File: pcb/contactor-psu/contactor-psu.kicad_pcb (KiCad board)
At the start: 2 copper layers, 44.1 x 24 mm, 4 parts, among them J1 Conn_01x02_Socket

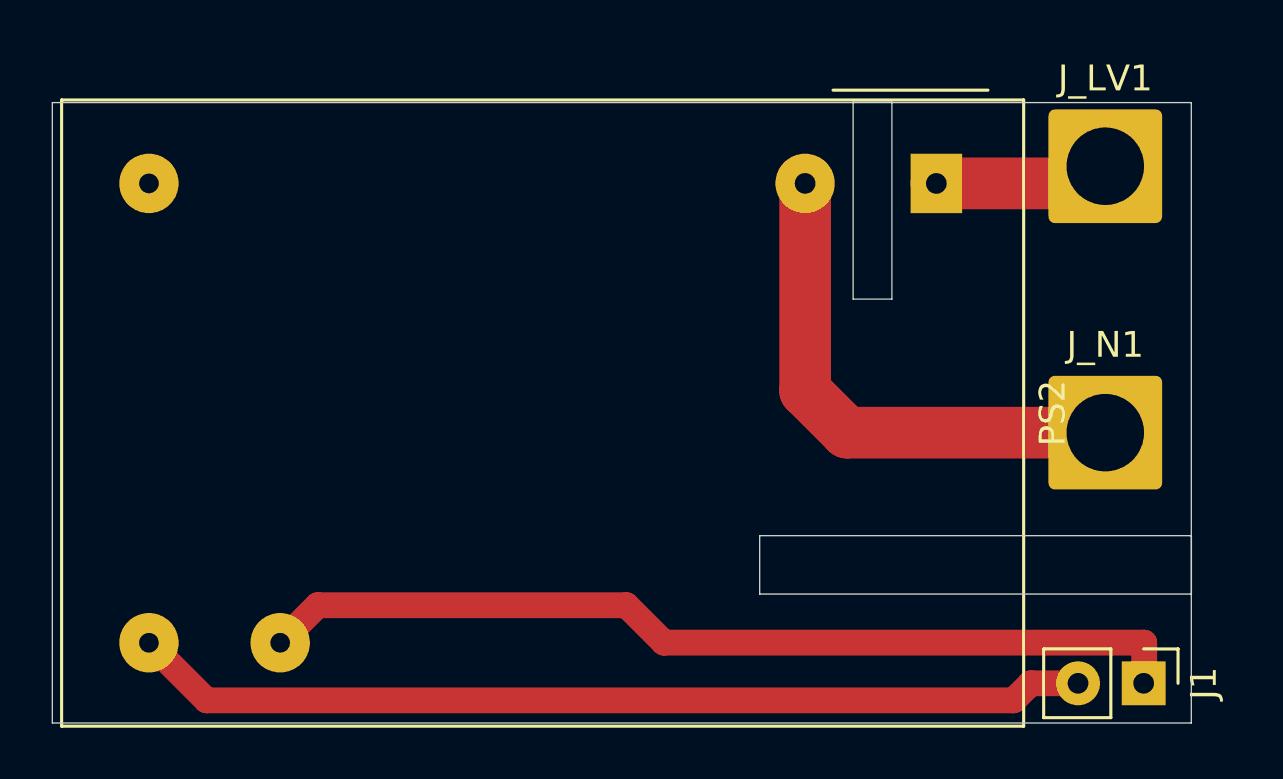
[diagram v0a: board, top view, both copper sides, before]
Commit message: Fixes to relief, JST connectors for SMT board
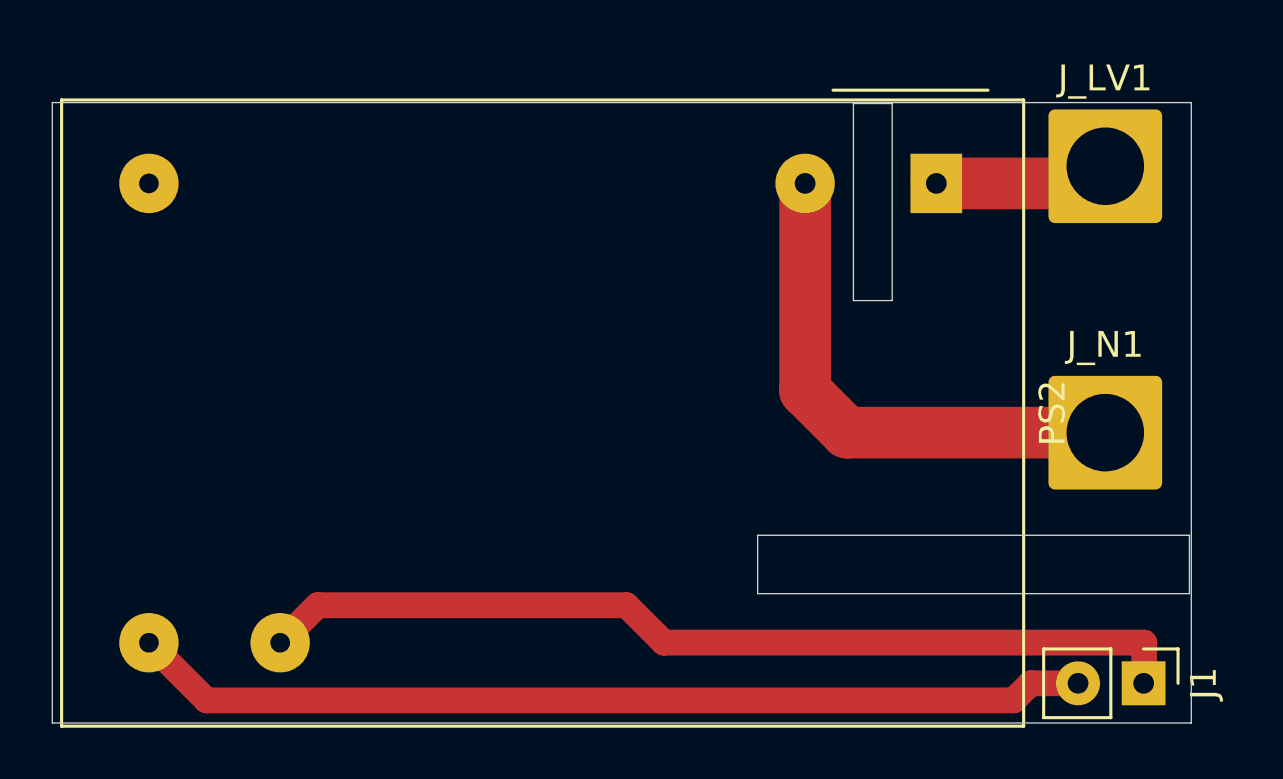
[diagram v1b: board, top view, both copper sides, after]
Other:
- outline, holes or cut-outs redrawn
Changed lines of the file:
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@@
 			(size 4.4 4.4)
 			(drill 3)
-			(layers "*.Cu" "*.Mask")
+			(layers "*.Cu" "*.Mask" "In1.Cu" "In2.Cu" "In3.Cu" "In4.Cu" "In5.Cu" "In6.Cu"
+				"In7.Cu" "In8.Cu" "In9.Cu" "In10.Cu" "In11.Cu" "In12.Cu" "In13.Cu" "In14.Cu"
+				"In15.Cu" "In16.Cu" "In17.Cu" "In18.Cu" "In19.Cu" "In20.Cu" "In21.Cu"
+				"In22.Cu" "In23.Cu" "In24.Cu" "In25.Cu" "In26.Cu" "In27.Cu" "In28.Cu"
+				"In29.Cu" "In30.Cu"
+			)
 			(remove_unused_layers no)
 			(roundrect_rratio 0.056818)
@@
 			(size 2.3 2)
 			(drill 0.8)
-			(layers "*.Cu" "*.Mask")
+			(layers "*.Cu" "*.Mask" "In1.Cu" "In2.Cu" "In3.Cu" "In4.Cu" "In5.Cu" "In6.Cu"
+				"In7.Cu" "In8.Cu" "In9.Cu" "In10.Cu" "In11.Cu" "In12.Cu" "In13.Cu" "In14.Cu"
+				"In15.Cu" "In16.Cu" "In17.Cu" "In18.Cu" "In19.Cu" "In20.Cu" "In21.Cu"
+				"In22.Cu" "In23.Cu" "In24.Cu" "In25.Cu" "In26.Cu" "In27.Cu" "In28.Cu"
+				"In29.Cu" "In30.Cu"
+			)
 			(remove_unused_layers no)
 			(net 3 "Net-(J_LV1-Pin_1)")
@@
 			(size 2.3 2.3)
 			(drill 0.8)
-			(layers "*.Cu" "*.Mask")
+			(layers "*.Cu" "*.Mask" "In1.Cu" "In2.Cu" "In3.Cu" "In4.Cu" "In5.Cu" "In6.Cu"
+				"In7.Cu" "In8.Cu" "In9.Cu" "In10.Cu" "In11.Cu" "In12.Cu" "In13.Cu" "In14.Cu"
+				"In15.Cu" "In16.Cu" "In17.Cu" "In18.Cu" "In19.Cu" "In20.Cu" "In21.Cu"
+				"In22.Cu" "In23.Cu" "In24.Cu" "In25.Cu" "In26.Cu" "In27.Cu" "In28.Cu"
+				"In29.Cu" "In30.Cu"
+			)
 			(remove_unused_layers no)
 			(net 4 "Net-(J_N1-Pin_1)")
@@
 			(size 2.3 2.3)
 			(drill 0.76)
-			(layers "*.Cu" "*.Mask")
+			(layers "*.Cu" "*.Mask" "In1.Cu" "In2.Cu" "In3.Cu" "In4.Cu" "In5.Cu" "In6.Cu"
+				"In7.Cu" "In8.Cu" "In9.Cu" "In10.Cu" "In11.Cu" "In12.Cu" "In13.Cu" "In14.Cu"
+				"In15.Cu" "In16.Cu" "In17.Cu" "In18.Cu" "In19.Cu" "In20.Cu" "In21.Cu"
+				"In22.Cu" "In23.Cu" "In24.Cu" "In25.Cu" "In26.Cu" "In27.Cu" "In28.Cu"
+				"In29.Cu" "In30.Cu"
+			)
 			(remove_unused_layers no)
 			(net 5 "unconnected-(PS2-NC-Pad5)")
@@
 			(size 2.3 2.3)
 			(drill 0.76)
-			(layers "*.Cu" "*.Mask")
+			(layers "*.Cu" "*.Mask" "In1.Cu" "In2.Cu" "In3.Cu" "In4.Cu" "In5.Cu" "In6.Cu"
+				"In7.Cu" "In8.Cu" "In9.Cu" "In10.Cu" "In11.Cu" "In12.Cu" "In13.Cu" "In14.Cu"
+				"In15.Cu" "In16.Cu" "In17.Cu" "In18.Cu" "In19.Cu" "In20.Cu" "In21.Cu"
+				"In22.Cu" "In23.Cu" "In24.Cu" "In25.Cu" "In26.Cu" "In27.Cu" "In28.Cu"
+				"In29.Cu" "In30.Cu"
+			)
 			(remove_unused_layers no)
 			(net 1 "Net-(J1-Pin_2)")
@@
 			(size 2.3 2.3)
 			(drill 0.76)
-			(layers "*.Cu" "*.Mask")
+			(layers "*.Cu" "*.Mask" "In1.Cu" "In2.Cu" "In3.Cu" "In4.Cu" "In5.Cu" "In6.Cu"
+				"In7.Cu" "In8.Cu" "In9.Cu" "In10.Cu" "In11.Cu" "In12.Cu" "In13.Cu" "In14.Cu"
+				"In15.Cu" "In16.Cu" "In17.Cu" "In18.Cu" "In19.Cu" "In20.Cu" "In21.Cu"
+				"In22.Cu" "In23.Cu" "In24.Cu" "In25.Cu" "In26.Cu" "In27.Cu" "In28.Cu"
+				"In29.Cu" "In30.Cu"
+			)
 			(remove_unused_layers no)
 			(net 2 "Net-(J1-Pin_1)")
@@
 			(size 1.7 1.7)
 			(drill 0.8)
-			(layers "*.Cu" "*.Mask")
+			(layers "*.Cu" "*.Mask" "In1.Cu" "In2.Cu" "In3.Cu" "In4.Cu" "In5.Cu" "In6.Cu"
+				"In7.Cu" "In8.Cu" "In9.Cu" "In10.Cu" "In11.Cu" "In12.Cu" "In13.Cu" "In14.Cu"
+				"In15.Cu" "In16.Cu" "In17.Cu" "In18.Cu" "In19.Cu" "In20.Cu" "In21.Cu"
+				"In22.Cu" "In23.Cu" "In24.Cu" "In25.Cu" "In26.Cu" "In27.Cu" "In28.Cu"
+				"In29.Cu" "In30.Cu"
+			)
 			(remove_unused_layers no)
 			(net 2 "Net-(J1-Pin_1)")
@@
 			(size 1.7 1.7)
 			(drill 0.8)
-			(layers "*.Cu" "*.Mask")
+			(layers "*.Cu" "*.Mask" "In1.Cu" "In2.Cu" "In3.Cu" "In4.Cu" "In5.Cu" "In6.Cu"
+				"In7.Cu" "In8.Cu" "In9.Cu" "In10.Cu" "In11.Cu" "In12.Cu" "In13.Cu" "In14.Cu"
+				"In15.Cu" "In16.Cu" "In17.Cu" "In18.Cu" "In19.Cu" "In20.Cu" "In21.Cu"
+				"In22.Cu" "In23.Cu" "In24.Cu" "In25.Cu" "In26.Cu" "In27.Cu" "In28.Cu"
+				"In29.Cu" "In30.Cu"
+			)
 			(remove_unused_layers no)
 			(net 1 "Net-(J1-Pin_2)")
@@
 			(size 4.4 4.4)
 			(drill 3)
-			(layers "*.Cu" "*.Mask")
+			(layers "*.Cu" "*.Mask" "In1.Cu" "In2.Cu" "In3.Cu" "In4.Cu" "In5.Cu" "In6.Cu"
+				"In7.Cu" "In8.Cu" "In9.Cu" "In10.Cu" "In11.Cu" "In12.Cu" "In13.Cu" "In14.Cu"
+				"In15.Cu" "In16.Cu" "In17.Cu" "In18.Cu" "In19.Cu" "In20.Cu" "In21.Cu"
+				"In22.Cu" "In23.Cu" "In24.Cu" "In25.Cu" "In26.Cu" "In27.Cu" "In28.Cu"
+				"In29.Cu" "In30.Cu"
+			)
 			(remove_unused_layers no)
 			(roundrect_rratio 0.056818)
@@
 	)
 	(gr_rect
-		(start 31 7.3716)
-		(end 32.5 15)
+		(start 31.01 7.4258)
+		(end 32.51 15.0542)
 		(stroke
 			(width 0.05)
@@
 	)
 	(gr_rect
-		(start 27.3812 24.1554)
-		(end 44.0944 26.416)
+		(start 27.3034 24.1394)
+		(end 44.0166 26.4)
 		(stroke
 			(width 0.05)

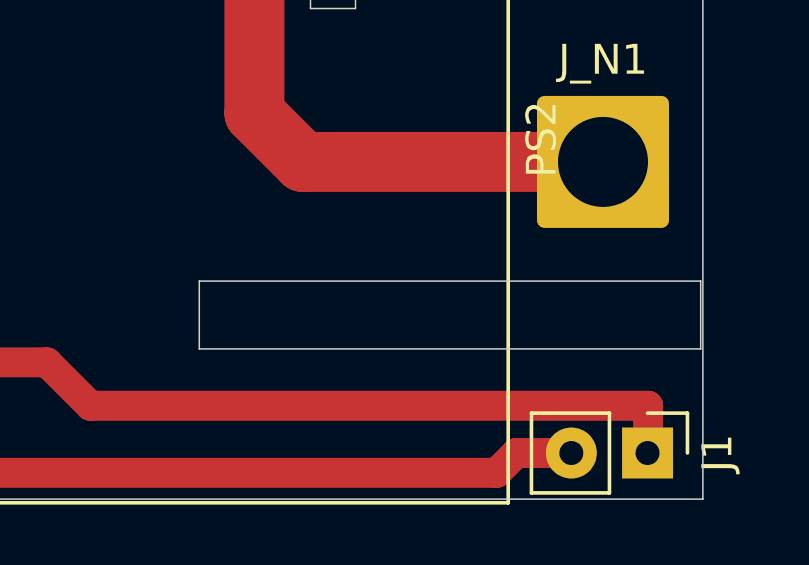
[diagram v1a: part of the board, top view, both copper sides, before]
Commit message: Clearance fixes for contactor interface relay
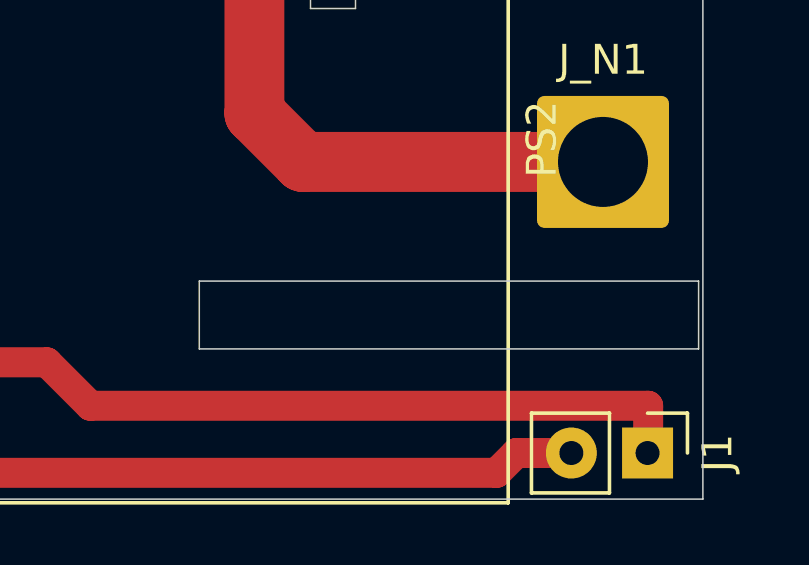
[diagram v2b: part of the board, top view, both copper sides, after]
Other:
- outline, holes or cut-outs redrawn
